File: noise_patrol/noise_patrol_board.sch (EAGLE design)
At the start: 16 parts, among them IC1 4511D, Q1 TIP31C, U1 OPA345NA/3K

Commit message: Starting to Rearrange the board
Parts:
- added C2: 2.2\muF, SparkFun-Capacitors:0.22UF-0603-50V-10%
- added C3: 15pF, SparkFun-Capacitors:0.22UF-0603-50V-10%
- added R10, R11, R12: 100k, rcl:R-US_M1206
- added R9: 75k, rcl:R-US_M1206
- added X1: (no value), con-wago-508:W237-09P
- R8: value (none) -> 13.7k
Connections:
- removed net +5V: U1.V+
- new net N$21: C1.2, C2.1, R9.1, U1.-IN
- new net N$22: B1.*D3, R12.1
- new net N$23: Q1.B, R12.2
- new net N$24: C3.1, R10.2, R11.1, U1.+IN
- new net N$25: D1.A, Q1.C, X1-1.KL
- new net N$26: D1.C, X1-2.KL
- net 5V: now also R10.1, U1.V+
- net GND: now also C3.2, MK1.2, Q1.E, R11.2
- net N$18: now also C2.2, R9.2
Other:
- moved on the sheet: C1, D1, MK1, Q1, R8

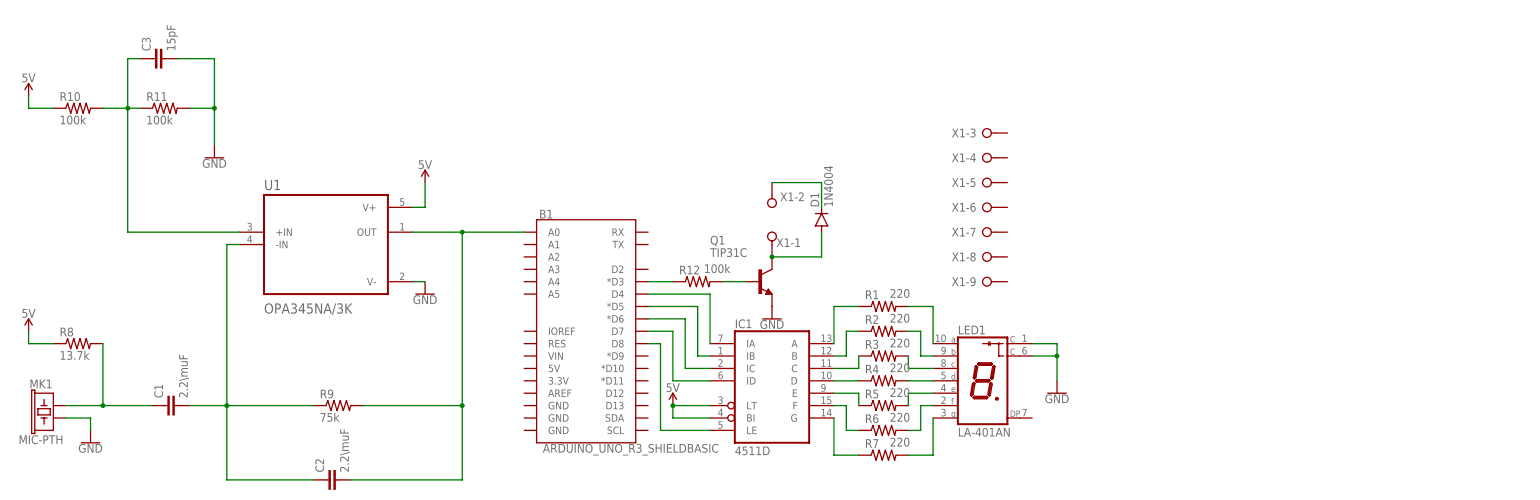
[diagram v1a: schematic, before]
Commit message: Finished getting everything on to the board
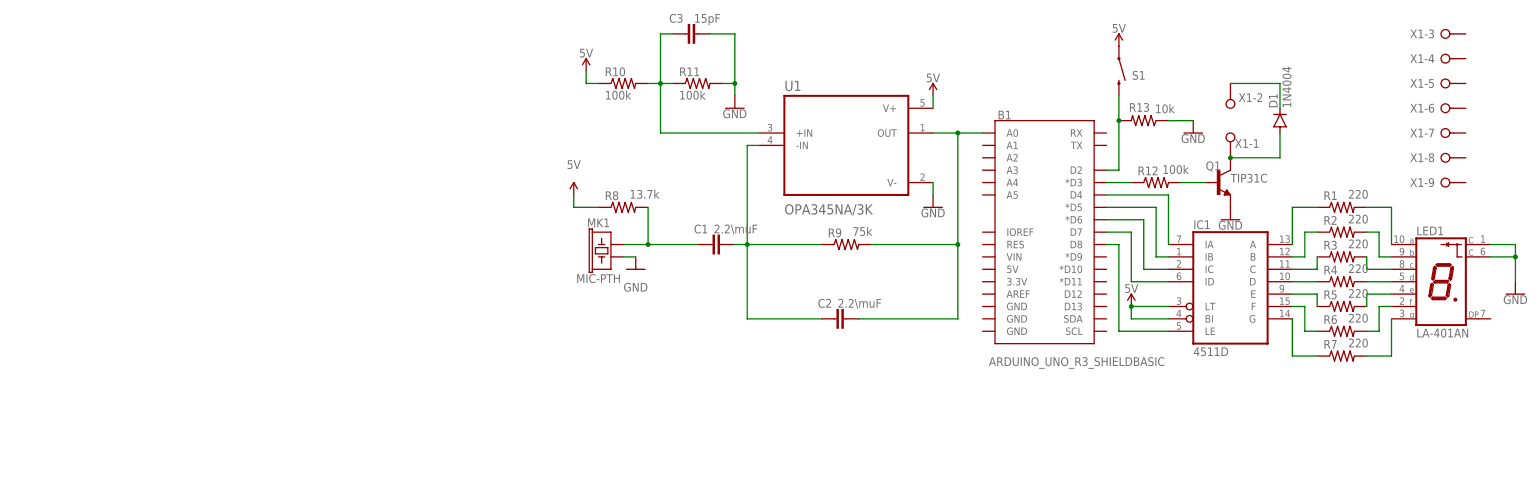
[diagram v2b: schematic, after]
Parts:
- added R13: 10k, rcl:R-US_M1206
- added S1: MOMENTARY-SWITCH-SPST-PTH-6.0MM, SparkFun-Switches:MOMENTARY-SWITCH-SPST-PTH-6.0MM
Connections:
- new net N$27: B1.D2, R13.2, S1.2
- net 5V: now also S1.1
- net GND: now also R13.1
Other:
- moved on the sheet: B1, C1, C2, C3, D1, IC1, LED1, MK1, Q1, R1, R10, R11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

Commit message: Finished
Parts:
- S1: value MOMENTARY-SWITCH-SPST-PTH-6.0MM -> Reset button
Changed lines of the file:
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@@
 <part name="SUPPLY5" library="SparkFun-PowerSymbols" deviceset="5V" device=""/>
 <part name="R13" library="rcl" library_urn="urn:adsk.eagle:library:334" deviceset="R-US_" device="M1206" package3d_urn="urn:adsk.eagle:package:23566/2" value="10k"/>
-<part name="S1" library="SparkFun-Switches" deviceset="MOMENTARY-SWITCH-SPST" device="-PTH-6.0MM"/>
+<part name="S1" library="SparkFun-Switches" deviceset="MOMENTARY-SWITCH-SPST" device="-PTH-6.0MM" value="Reset button "/>
 <part name="GND6" library="SparkFun-PowerSymbols" deviceset="GND" device=""/>
 </parts>

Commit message: Final
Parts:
- R12: value 100k -> 1k
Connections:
- removed net N$26: D1.C, X1-2.KL
- net 5V: now also D1.C, X1-2.KL
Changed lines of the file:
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@@
 <part name="GND4" library="SparkFun-PowerSymbols" deviceset="GND" device=""/>
 <part name="GND5" library="SparkFun-PowerSymbols" deviceset="GND" device=""/>
-<part name="R12" library="rcl" library_urn="urn:adsk.eagle:library:334" deviceset="R-US_" device="M1206" package3d_urn="urn:adsk.eagle:package:23566/2" value="100k"/>
+<part name="R12" library="rcl" library_urn="urn:adsk.eagle:library:334" deviceset="R-US_" device="M1206" package3d_urn="urn:adsk.eagle:package:23566/2" value="1k"/>
 <part name="X1" library="con-wago-508" library_urn="urn:adsk.eagle:library:196" deviceset="W237-09P" device="" package3d_urn="urn:adsk.eagle:package:10748/1"/>
 <part name="SUPPLY5" library="SparkFun-PowerSymbols" deviceset="5V" device=""/>
@@
 <part name="S1" library="SparkFun-Switches" deviceset="MOMENTARY-SWITCH-SPST" device="-PTH-6.0MM" value="Reset button "/>
 <part name="GND6" library="SparkFun-PowerSymbols" deviceset="GND" device=""/>
+<part name="SUPPLY6" library="SparkFun-PowerSymbols" deviceset="5V" device=""/>
+<part name="GND7" library="SparkFun-PowerSymbols" deviceset="GND" device=""/>
+<part name="SUPPLY7" library="SparkFun-PowerSymbols" deviceset="5V" device=""/>
 </parts>
 <sheets>
@@
 <attribute name="VALUE" x="149.86" y="55.626" size="1.778" layer="96" font="vector" align="top-center"/>
 </instance>
+<instance part="SUPPLY6" gate="G$1" x="167.64" y="2.54" smashed="yes">
+<attribute name="VALUE" x="167.64" y="5.334" size="1.778" layer="96" font="vector" align="bottom-center"/>
+</instance>
+<instance part="GND7" gate="1" x="167.64" y="-2.54" smashed="yes">
+<attribute name="VALUE" x="167.64" y="-2.794" size="1.778" layer="96" font="vector" align="top-center"/>
+</instance>
+<instance part="SUPPLY7" gate="G$1" x="162.56" y="68.58" smashed="yes">
+<attribute name="VALUE" x="162.56" y="71.374" size="1.778" layer="96" font="vector" align="bottom-center"/>
+</instance>
 </instances>
 <busses>
@@
 <wire x1="22.86" y1="43.18" x2="22.86" y2="40.64" width="0.1524" layer="91"/>
 <wire x1="22.86" y1="40.64" x2="27.94" y2="40.64" width="0.1524" layer="91"/>
+</segment>
+<segment>
+<pinref part="D1" gate="1" pin="C"/>
+<wire x1="167.64" y1="60.96" x2="167.64" y2="66.04" width="0.1524" layer="91"/>
+<wire x1="167.64" y1="66.04" x2="162.56" y2="66.04" width="0.1524" layer="91"/>
+<pinref part="X1" gate="-2" pin="KL"/>
+<pinref part="SUPPLY7" gate="G$1" pin="5V"/>
+<wire x1="162.56" y1="66.04" x2="157.48" y2="66.04" width="0.1524" layer="91"/>
+<wire x1="162.56" y1="68.58" x2="162.56" y2="66.04" width="0.1524" layer="91"/>
+<junction x="162.56" y="66.04"/>
 </segment>
 </net>
@@
 </segment>
 </net>
-<net name="N$26" class="0">
-<segment>
-<pinref part="D1" gate="1" pin="C"/>
-<wire x1="167.64" y1="60.96" x2="167.64" y2="66.04" width="0.1524" layer="91"/>
-<wire x1="167.64" y1="66.04" x2="157.48" y2="66.04" width="0.1524" layer="91"/>
-<pinref part="X1" gate="-2" pin="KL"/>
-</segment>
-</net>
